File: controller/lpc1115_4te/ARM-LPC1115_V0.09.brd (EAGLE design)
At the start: 66 x 57.9 mm, 53 parts, among them IC1 LPC1115, IC2 MC34063AP, IC3 MCP1702-33, Q1 BC557B, Q3 BC640C, Q4 12MHz, T1 BC547C

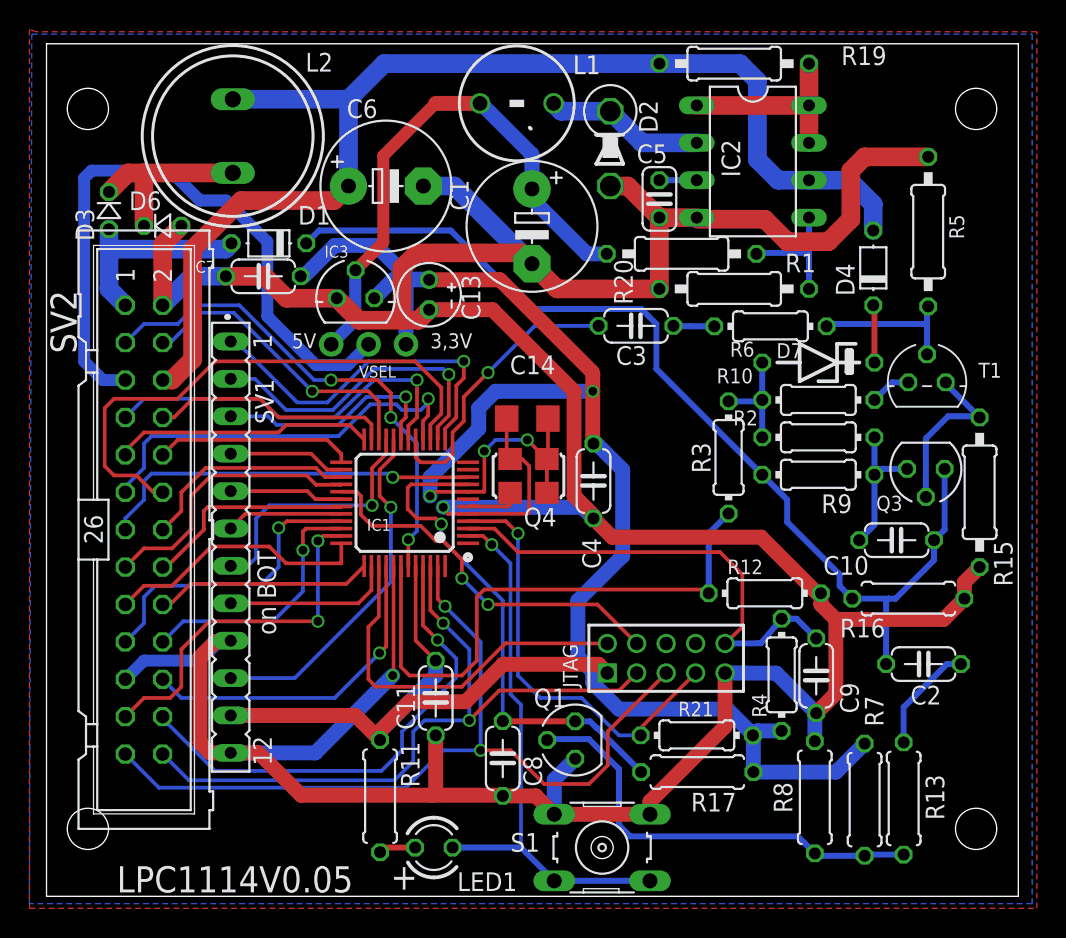
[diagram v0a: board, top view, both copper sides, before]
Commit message: Small changes in 0.08, new version 0.09 added
A new layout 0.09 has been created which has improved routing for the
supplies and changed pinout.
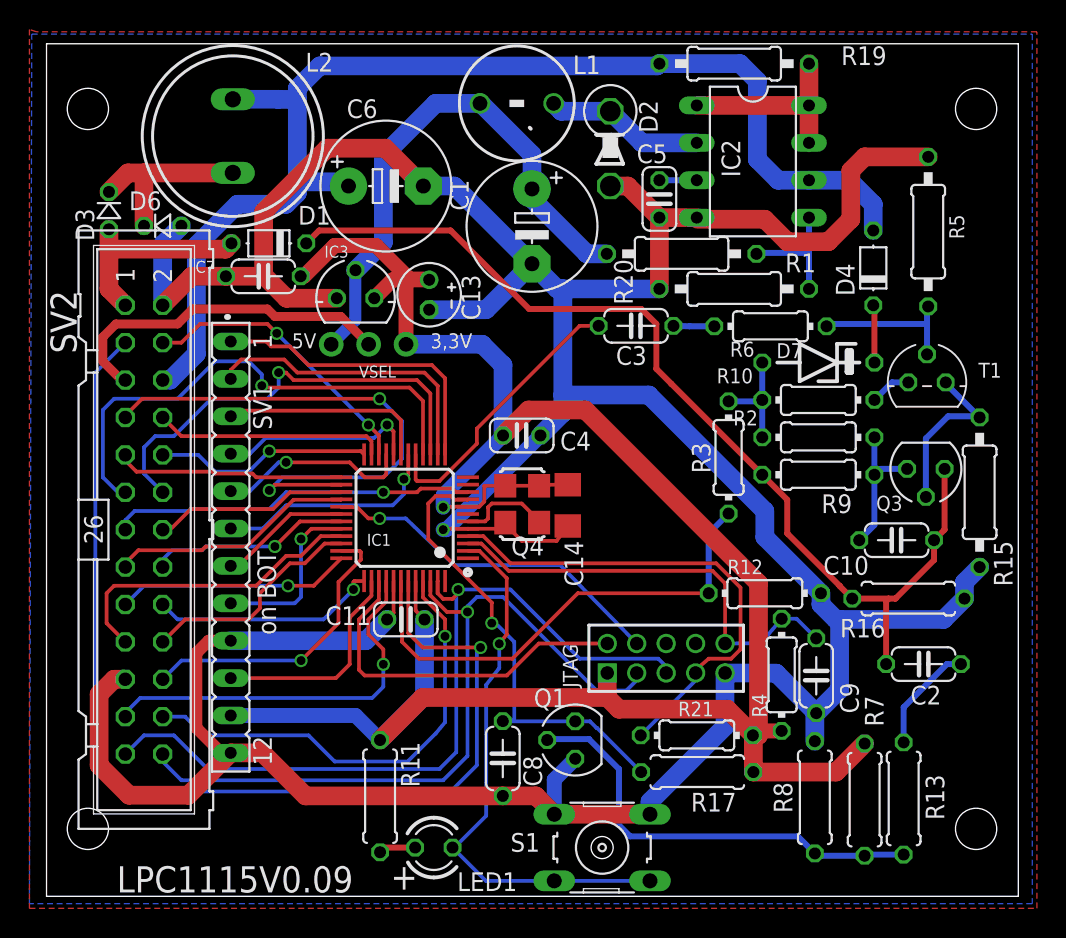
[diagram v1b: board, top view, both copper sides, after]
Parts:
- C11, C4: device rcl:C050-024X044 -> rcl:C025-024X044
- moved C14 6.50 mm to (36.4, 27.1), turned to 270 degrees
- moved C4 5.77 mm to (33.3, 31.8), turned to 180 degrees
- moved C11 5.71 mm to (25.4, 19.3), turned to 0 degrees
- moved Q4 1.97 mm to (33.3, 27.1), turned to 270 degrees
- moved IC1 1.02 mm to (25.3, 26.2)
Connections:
- net IO1: now also IC1.26; no longer IC1.18
- net IO11: now also IC1.35; no longer IC1.40
- net IO12: now also IC1.40; no longer IC1.35
- net IO3: now also IC1.25; no longer IC1.24
- net IO4: now also IC1.24; no longer IC1.25
- net LT4: now also IC1.20; no longer IC1.26
- net LT5: now also IC1.21; no longer IC1.30
- net LT6: now also IC1.18; no longer IC1.32
- net LT7: now also IC1.30; no longer IC1.21
- net LT8: now also IC1.32; no longer IC1.38
- net LT9: now also IC1.38; no longer IC1.20
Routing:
- net PWM: track 34.3 -> 73.6 mm, vias 3 -> 1
- net VCC_A: track 44.3 -> 23.5 mm
- net VCC_3V3: track 159.4 -> 147.7 mm, vias 4 -> 1
- net IO1: track 26.2 -> 37.5 mm, vias 1 -> 2
- net LT9: track 24.0 -> 14.7 mm, vias 1 -> 0
- net LT7: track 17.8 -> 8.97 mm, vias 1 -> 0
- net LT6: track 7.92 -> 15.5 mm, vias 0 -> 1
- net SDA: track 27.8 -> 34.8 mm
- net SCL: track 37.4 -> 30.5 mm, vias 0 -> 1
- net BUS_V: track 39.0 -> 33.3 mm
- net LT4: track 7.96 -> 13.6 mm, vias 0 -> 1
- net LT5: track 7.74 -> 13.2 mm, vias 0 -> 1
- net ISP_EN: track 29.2 -> 33.7 mm, vias 1 -> 0
- net GND: track 274.2 -> 270.3 mm, vias 2 -> 1
- net IO15: track 48.7 -> 51.7 mm, vias 2 -> 1
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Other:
- board text added: "LPC1115V0.09"
- board text removed: "LPC1114V0.05"

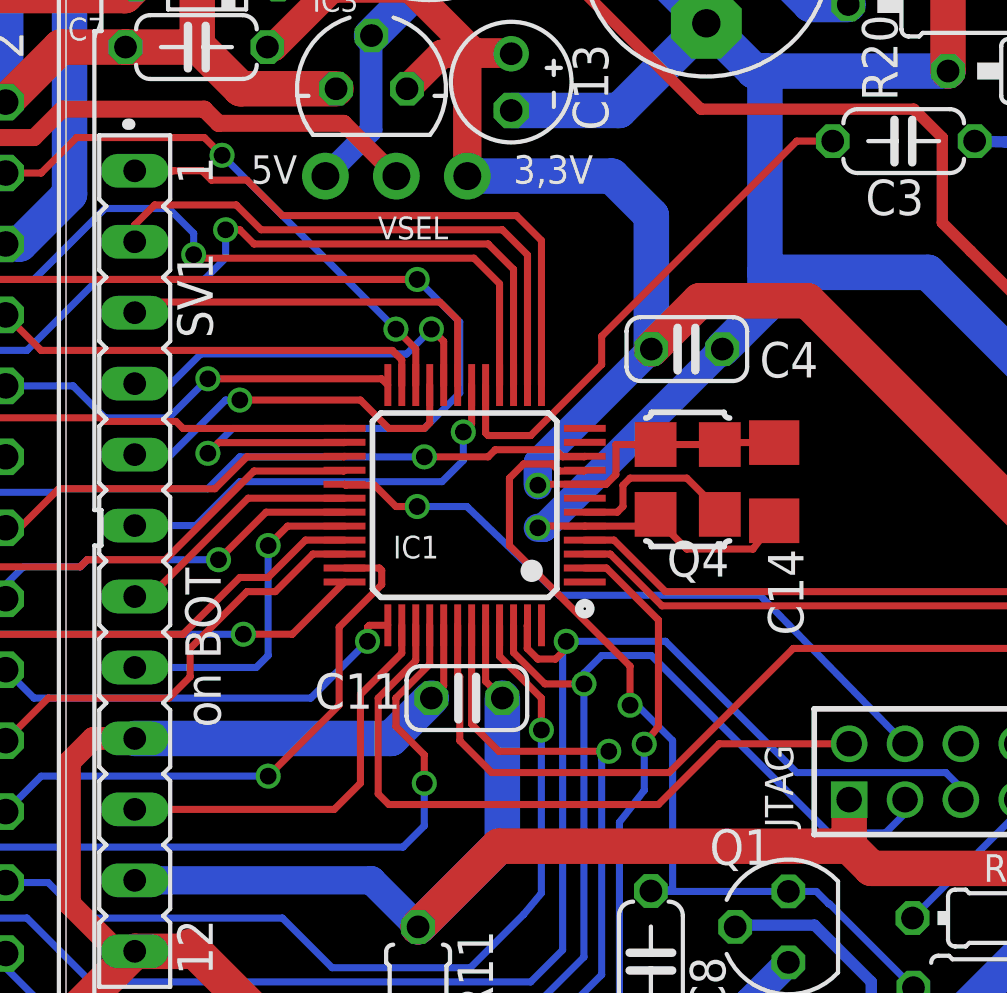
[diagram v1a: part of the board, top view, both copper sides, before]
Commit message: C near Osci moved
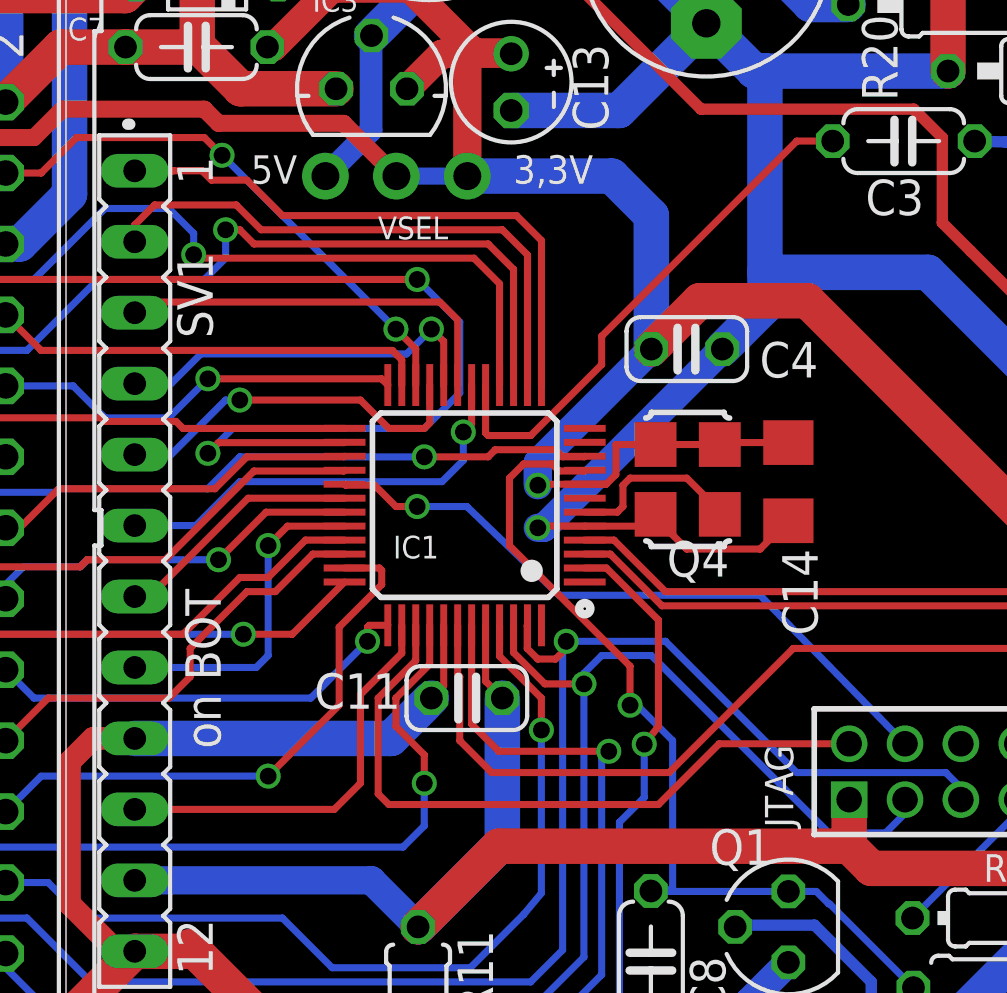
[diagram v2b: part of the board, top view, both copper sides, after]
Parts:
- moved C14 0.51 mm to (36.9, 27.1)
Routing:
- net VCC_3V3: track 147.7 -> 150.7 mm
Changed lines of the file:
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@@
 <?xml version="1.0" encoding="utf-8"?>
 <!DOCTYPE eagle SYSTEM "eagle.dtd">
-<eagle version="6.4">
+<eagle version="6.5.0">
 <drawing>
 <settings>
@@
 <text x="21.8281" y="2.54" size="1.778" layer="25" rot="R180">LPC1115V0.09</text>
 <text x="43.8944" y="1.8256" size="1.016" layer="27">auf Lötseite:</text>
-<text x="15.3194" y="23.9713" size="1.27" layer="21" font="vector" ratio="10" rot="R270">on BOT</text>
+<text x="15.3194" y="23.2093" size="1.27" layer="21" font="vector" ratio="10" rot="R270">on BOT</text>
 <text x="24.3681" y="0.9525" size="1.778" layer="21">+</text>
 <text x="17.6689" y="37.719" size="1.016" layer="21">5V</text>
@@
 <attribute name="VALUE" x="36.909375" y="30.5753" size="1.27" layer="27" rot="R180"/>
 </element>
-<element name="C14" library="rcl" package="C1206" value="10n" x="36.4013" y="27.051025" smashed="yes" rot="R270">
-<attribute name="NAME" x="36.1791" y="24.638025" size="1.27" layer="25" rot="R270"/>
-<attribute name="VALUE" x="37.5919" y="28.622725" size="1.27" layer="27" rot="R270"/>
+<element name="C14" library="rcl" package="C1206" value="10n" x="36.9093" y="27.051025" smashed="yes" rot="R270">
+<attribute name="NAME" x="36.6871" y="24.638025" size="1.27" layer="25" rot="R270"/>
+<attribute name="VALUE" x="38.0999" y="28.622725" size="1.27" layer="27" rot="R270"/>
 </element>
 <element name="R3" library="rcl" package="0204/7" value="91k" x="47.3235" y="30.3053" smashed="yes" rot="R270">
@@
 <attribute name="OC_FARNELL" value="unknown" x="7.62" y="25.4" size="1.778" layer="27" rot="R270" display="off"/>
 <attribute name="NAME" x="1.27" y="41.656" size="1.778" layer="25" ratio="10" rot="R270"/>
-<attribute name="VALUE" x="12.7" y="24.13" size="1.778" layer="27" ratio="10" rot="R270"/>
+<attribute name="VALUE" x="3.302" y="23.368" size="1.778" layer="27" ratio="10" rot="R270"/>
 </element>
 <element name="JTAG" library="pinhead-2" package="2X05M" value="J" x="43.08475" y="16.66875"/>
@@
 <wire x1="54.61" y1="19.304" x2="53.594" y2="20.32" width="1.27" layer="16"/>
 <wire x1="53.594" y1="20.32" x2="53.594" y2="21.082" width="1.27" layer="16"/>
-<wire x1="36.4013" y1="25.651025" x2="35.642275" y2="24.638" width="0.254" layer="1"/>
-<wire x1="35.642275" y1="24.638" x2="33.274" y2="24.638" width="0.254" layer="1"/>
+<wire x1="36.9093" y1="25.651025" x2="35.896275" y2="24.638" width="0.254" layer="1"/>
+<wire x1="35.896275" y1="24.638" x2="33.274" y2="24.638" width="0.254" layer="1"/>
 <wire x1="33.274" y1="24.638" x2="32.031625" y2="25.880375" width="0.254" layer="1"/>
 <wire x1="32.031625" y1="25.880375" x2="32.1557" y2="25.880375" width="0.254" layer="1"/>
@@
 <wire x1="25.415875" y1="42.418" x2="25.654" y2="42.418" width="1.016" layer="1"/>
 <contactref element="C11" pad="2"/>
-<wire x1="36.4013" y1="28.451025" x2="34.0747" y2="28.451025" width="0.254" layer="1"/>
+<wire x1="36.9093" y1="28.451025" x2="34.0747" y2="28.451025" width="0.254" layer="1"/>
 <wire x1="34.0747" y1="28.451025" x2="34.4557" y2="28.380375" width="0.254" layer="1"/>
 <wire x1="34.4557" y1="28.380375" x2="32.1557" y2="28.380375" width="0.254" layer="1"/>
@@
 <wire x1="49.355375" y1="21.764625" x2="49.355375" y2="11.43" width="1.27" layer="1"/>
 <wire x1="49.355375" y1="11.43" x2="48.974375" y2="11.43" width="1.27" layer="1"/>
+<wire x1="25.415875" y1="37.988875" x2="22.86" y2="37.988875" width="0.6096" layer="16"/>
+<wire x1="22.86" y1="37.988875" x2="22.86" y2="37.973" width="0.4064" layer="16"/>
+<wire x1="22.86" y1="37.973" x2="25.415875" y2="37.988875" width="0" layer="19" extent="1-16"/>
 </signal>
 <signal name="VCC_A">
@@
 <wire x1="28.575" y1="3.81" x2="30.8356" y2="1.5494" width="0.254" layer="16"/>
 <wire x1="30.8356" y1="1.5494" x2="35.4838" y2="1.5494" width="0.254" layer="16"/>
-<wire x1="31.75" y1="17.653" x2="31.75" y2="16.002" width="0.254" layer="16"/>
-<wire x1="31.75" y1="16.002" x2="30.861" y2="14.859" width="0.254" layer="16"/>
+<wire x1="31.75" y1="17.653" x2="31.75" y2="15.748" width="0.254" layer="16"/>
+<wire x1="31.75" y1="15.748" x2="30.861" y2="14.859" width="0.254" layer="16"/>
 </signal>
 <signal name="IO6">
@@
 </signal>
 </signals>
+<errors>
+</errors>
 </board>
 </drawing>
